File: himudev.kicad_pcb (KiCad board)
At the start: 4 copper layers, 93.6 x 43.6 mm, 132 parts, among them J1 USB_C16PIN, J2 M20-8770642R, J3 M20-8770642R, J4 20021121-00010C4LF, J5 M20-8762042, Q1 IRLML6402, Q2 BSS214NW, Q3 BSS214NW, Q4 BSS214NW, Q5 BSS214NW, Q6 BSS214NW, U1 FT230XS, U2 MCP1726-3302ESN, U3 MIC5319-1.8YD5-TR, U4 IS25WP032D, U5 FE310-G002, U6 ICM-20948, U7 BMP388, X1 KX2132709Z, Y1 TSX-3225 16.0000MF18X-AC0

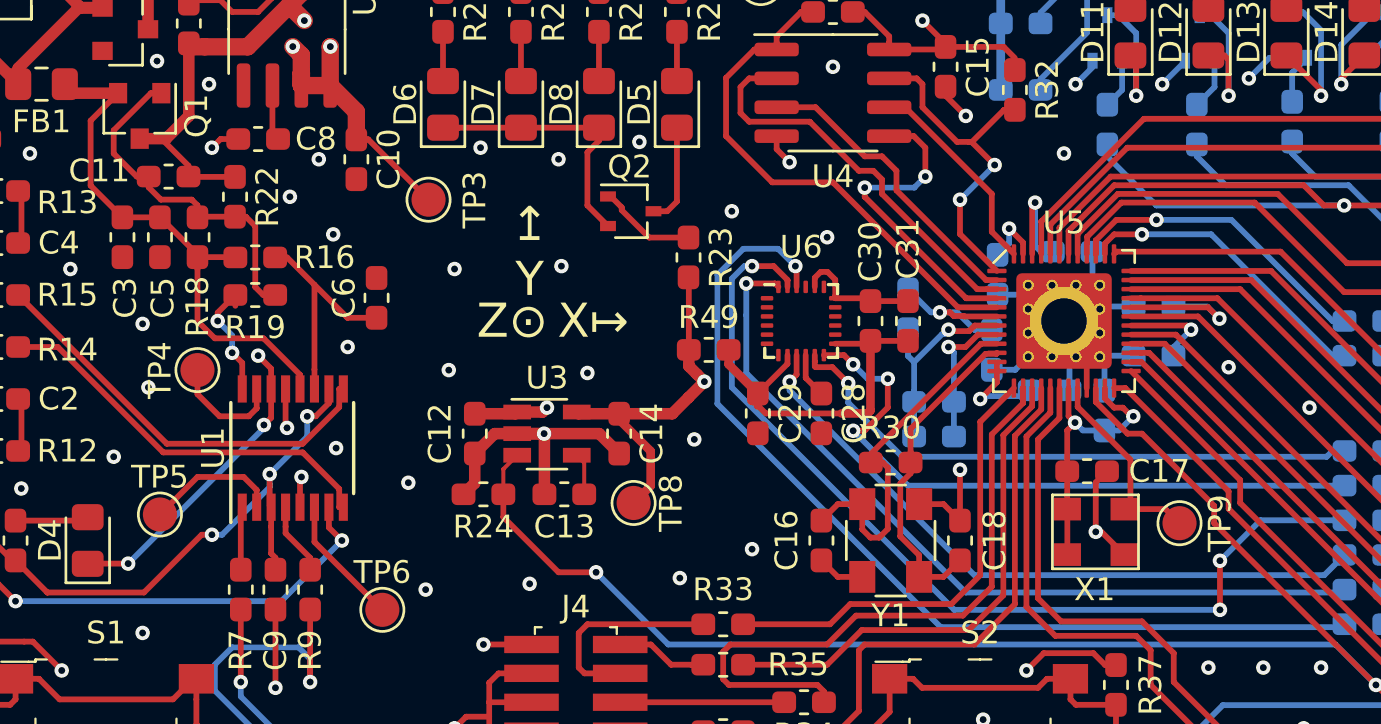
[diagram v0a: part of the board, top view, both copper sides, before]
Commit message: Made testpoint silkscreen more readable
Also, regenerated Gerber files.
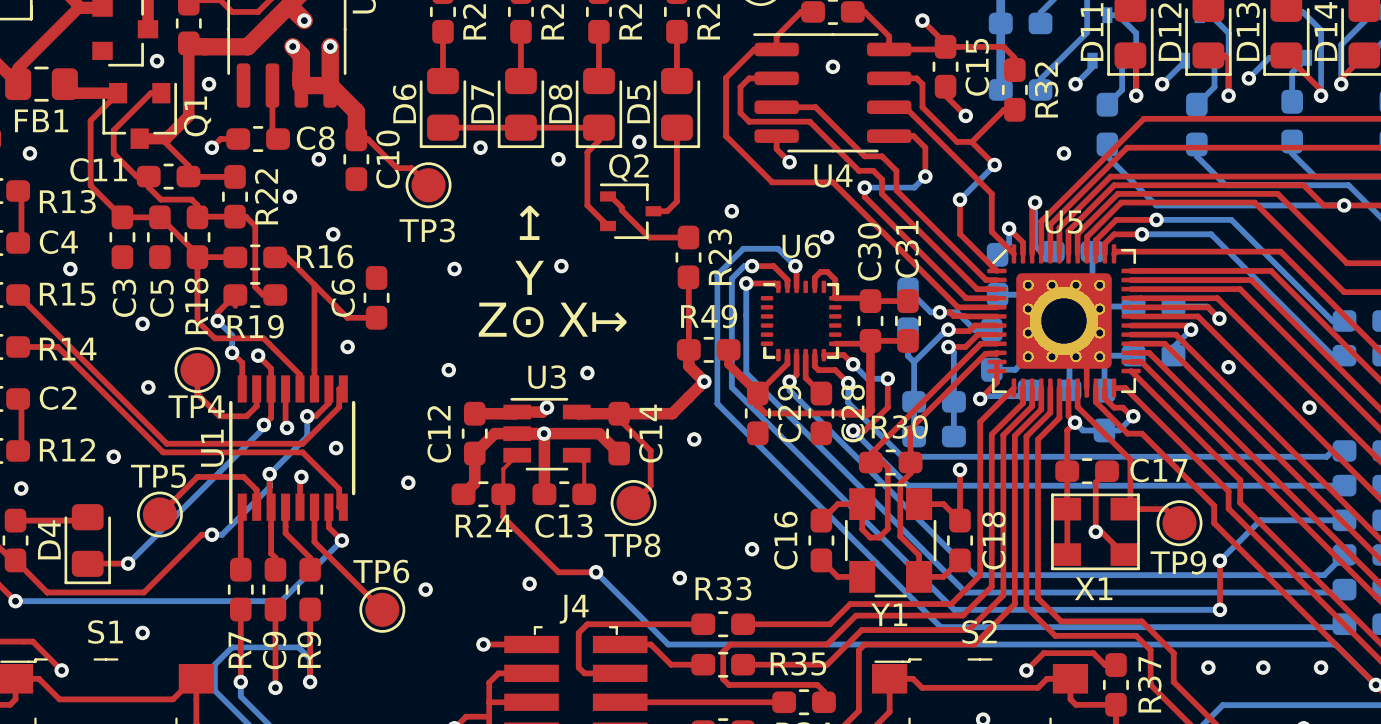
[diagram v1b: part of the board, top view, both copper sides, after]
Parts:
- moved TP3 0.64 mm to (136.0, 95.6), turned to 180 degrees
- turned TP4 to 180 degrees
- turned TP8 to 180 degrees
- turned TP9 to 180 degrees

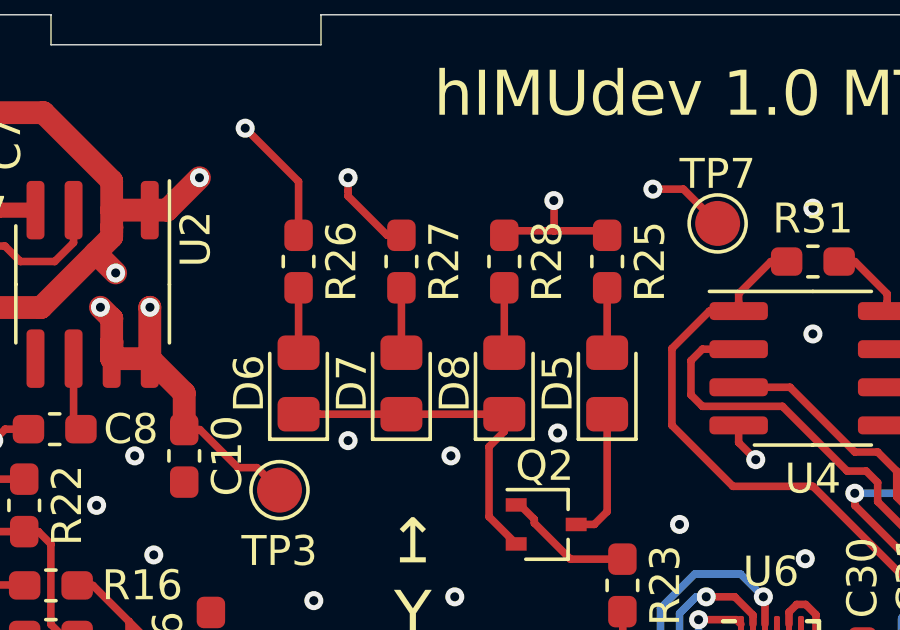
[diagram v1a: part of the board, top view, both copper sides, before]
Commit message: Reorder power LEDs in schematics, fix some USB-C DRC errors
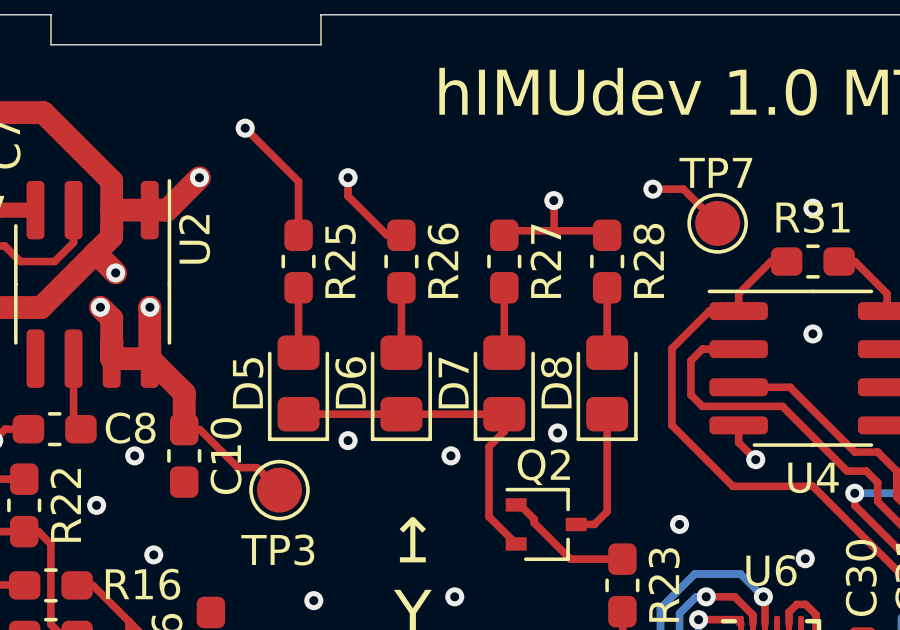
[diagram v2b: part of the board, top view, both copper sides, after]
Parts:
- J1: value USB_C16PIN -> USB-C-16PIN
- renumbered D6 to D5, D7 to D6, D8 to D7, D5 to D8, R26 to R25, R27 to R26, R28 to R27, R25 to R28

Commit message: Fix: exchange FTDI TX and RX diode colors
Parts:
- D3: value Green LTST-C170KGKT -> Orange LTST-C170KFKT
- D4: value Orange LTST-C170KFKT -> Green LTST-C170KGKT
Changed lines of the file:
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@@
       (effects (font (size 1 1) (thickness 0.15)))
     )
-    (fp_text value "Green LTST-C170KGKT" (at 0 1.65 90) (layer F.Fab)
+    (fp_text value "Orange LTST-C170KFKT" (at 0 1.65 90) (layer F.Fab)
       (effects (font (size 1 1) (thickness 0.15)))
     )
@@
       (effects (font (size 1 1) (thickness 0.15)))
     )
-    (fp_text value "Orange LTST-C170KFKT" (at 0 1.65 90) (layer F.Fab)
+    (fp_text value "Green LTST-C170KGKT" (at 0 1.65 90) (layer F.Fab)
       (effects (font (size 1 1) (thickness 0.15)))
     )

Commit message: Fix FTDI RX/TX diode designator
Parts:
- D3: value Orange LTST-C170KFKT -> Orange TX LTST-C170KFKT
- D4: value Green LTST-C170KGKT -> Green RX LTST-C170KGKT
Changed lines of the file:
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@@
       (effects (font (size 1 1) (thickness 0.15)))
     )
-    (fp_text value "Orange LTST-C170KFKT" (at 0 1.65 90) (layer F.Fab)
+    (fp_text value "Orange TX LTST-C170KFKT" (at 0 1.65 90) (layer F.Fab)
       (effects (font (size 1 1) (thickness 0.15)))
     )
@@
       (effects (font (size 1 1) (thickness 0.15)))
     )
-    (fp_text value "Green LTST-C170KGKT" (at 0 1.65 90) (layer F.Fab)
+    (fp_text value "Green RX LTST-C170KGKT" (at 0 1.65 90) (layer F.Fab)
       (effects (font (size 1 1) (thickness 0.15)))
     )

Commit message: Change resistor values to adjust LED brightness
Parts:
- R25: value 560 -> 1k
- R42: value 270 -> 560
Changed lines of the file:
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@@
       (effects (font (size 1 1) (thickness 0.15)))
     )
-    (fp_text value 560 (at 0 1.43 90) (layer F.Fab)
+    (fp_text value 1k (at 0 1.43 90) (layer F.Fab)
       (effects (font (size 1 1) (thickness 0.15)))
     )
@@
       (effects (font (size 1 1) (thickness 0.15)) (justify mirror))
     )
-    (fp_text value 270 (at 0 -1.43 180) (layer B.Fab)
-      (effects (font (size 1 1) (thickness 0.15)) (justify mirror))
-    )
+    (fp_text value 560 (at 0 -1.43 180) (layer B.Fab)
+      (effects (font (size 1 1) (thickness 0.15)) (justify mirror))
+    )

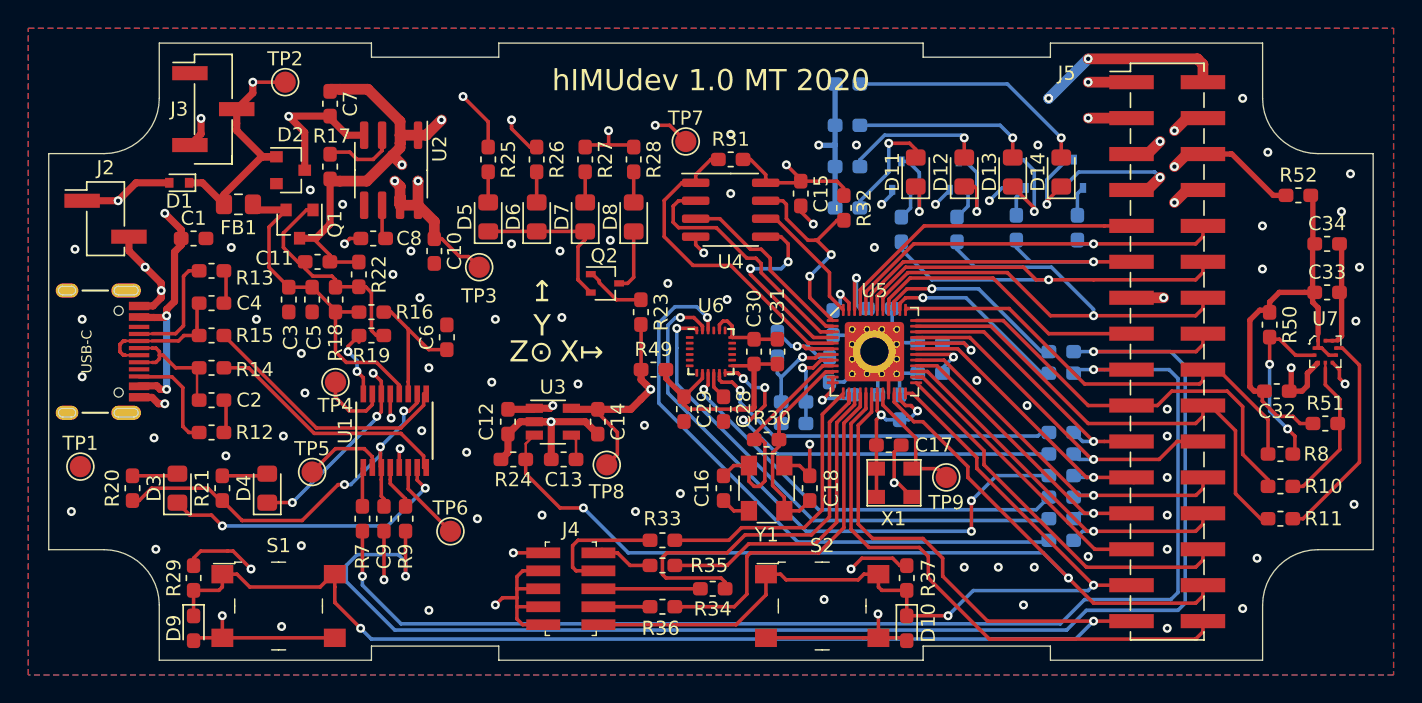
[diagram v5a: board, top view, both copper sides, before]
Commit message: Add 10k pull-downs on MCU LED outputs, improve layout
Pushed few traces, fixed DRC issue on one of the vias.
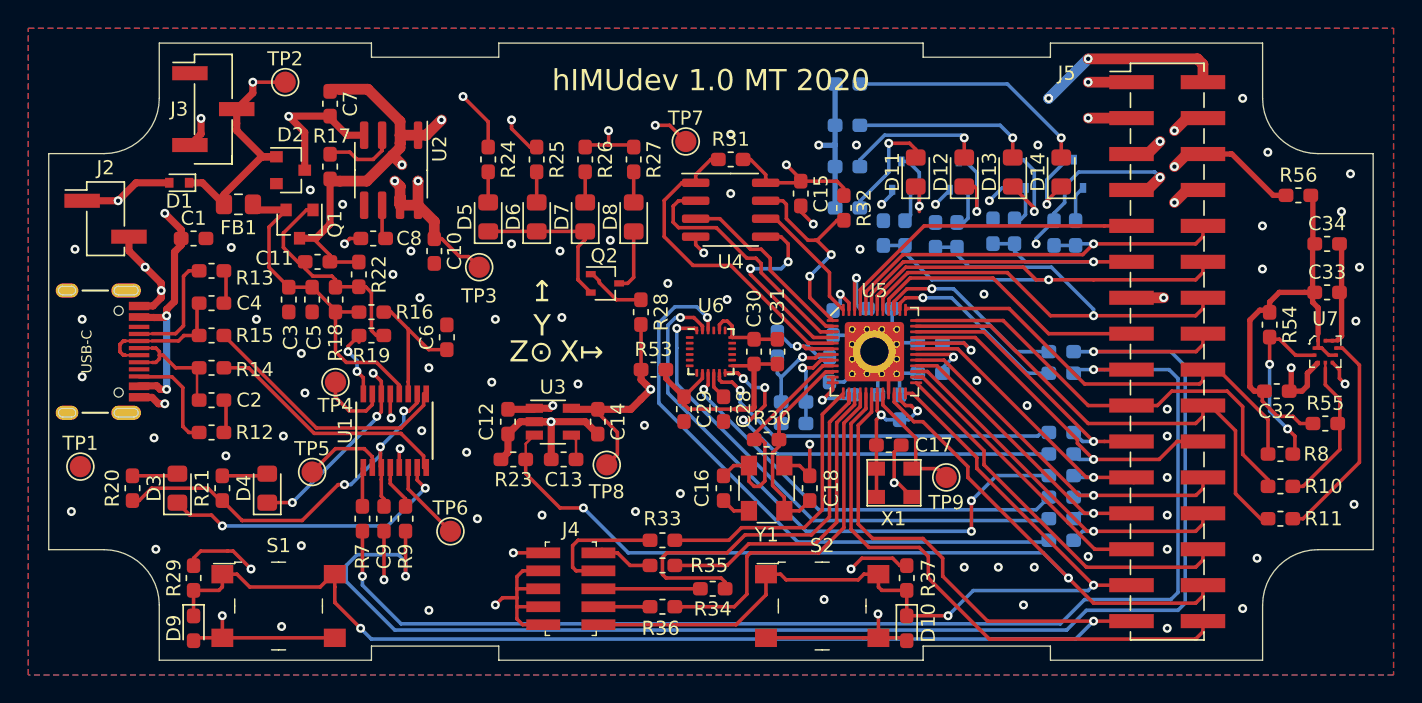
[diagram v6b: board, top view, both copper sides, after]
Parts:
- added R42: 10k, Resistor_SMD:R_0603_1608Metric_Pad1.05x0.95mm_HandSolder, B.Cu at (164.6, 93.2)
- added R45: 10k, Resistor_SMD:R_0603_1608Metric_Pad1.05x0.95mm_HandSolder, B.Cu at (168.3, 93.3)
- added R48: 10k, Resistor_SMD:R_0603_1608Metric_Pad1.05x0.95mm_HandSolder, B.Cu at (172.3, 93.1)
- added R51: 10k, Resistor_SMD:R_0603_1608Metric_Pad1.05x0.95mm_HandSolder, B.Cu at (176.7, 93.2)
- moved R50 0.40 mm to (178.2, 93.2)
- moved R44 0.38 mm to (169.8, 93.3)
- moved R41 0.36 mm to (166.1, 93.2)
- moved R47 0.28 mm to (173.9, 93.1)
- renumbered R24 to R23, R25 to R24, R26 to R25, R27 to R26, R28 to R27, R23 to R28, R42 to R43, R43 to R44, R44 to R46, R45 to R47, R46 to R49, R47 to R50, R48 to R52, R49 to R53, R50 to R54, R51 to R55, R52 to R56
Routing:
- net GND: track 197.5 -> 202.6 mm, vias 92 -> 94
- net /MCU_clk_reset/LED_4_YELLOW: track 28.7 -> 30.3 mm
- net /MCU_clk_reset/LED_3_BLUE: track 26.9 -> 28.4 mm
- net /MCU_clk_reset/LED_2_GREEN: track 38.8 -> 40.3 mm
- net /MCU_clk_reset/LED_1_RED: track 38.0 -> 39.2 mm
- net Net-(Q4-Pad1): track 2.26 -> 2.92 mm
- net Net-(Q5-Pad1): track 2.20 -> 2.79 mm

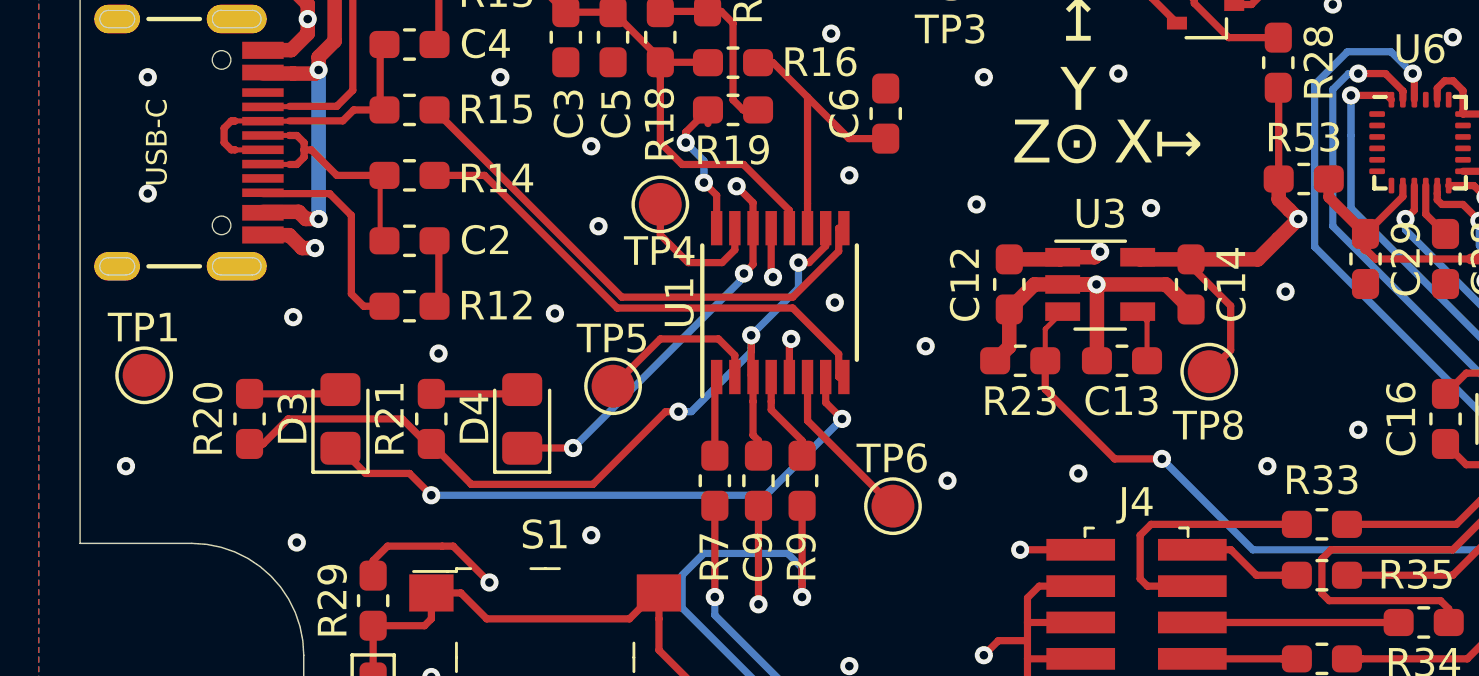
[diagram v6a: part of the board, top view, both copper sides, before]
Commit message: Switch places of D3 and D4
Also, fixed 1V8 via placement.
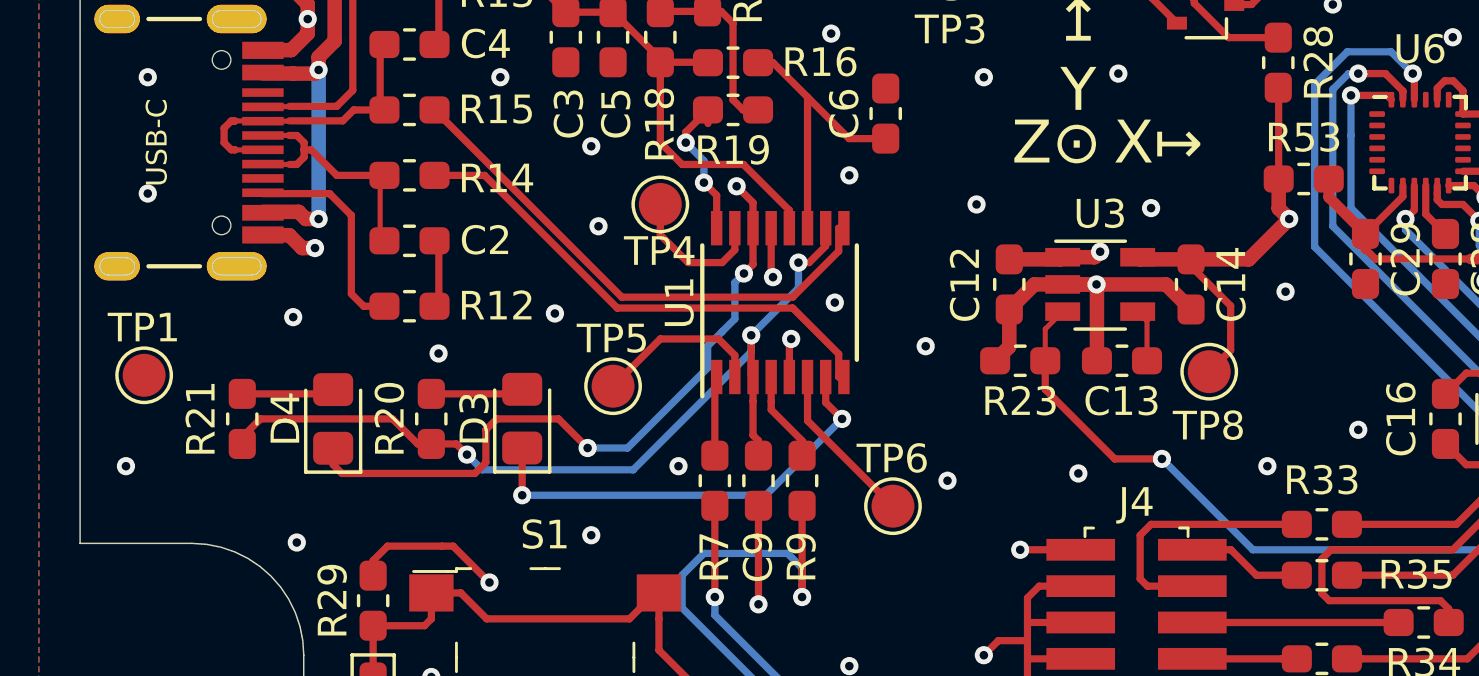
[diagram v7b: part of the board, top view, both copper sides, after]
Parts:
- moved D4 6.60 mm to (114.4, 111.3)
- moved R21 6.60 mm to (111.3, 111.3)
- moved D3 6.35 mm to (121.0, 111.2)
- moved R20 6.35 mm to (117.9, 111.3)
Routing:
- net Net-(D4-Pad1): track 13.8 -> 24.2 mm
- net Net-(D3-Pad1): track 21.0 -> 15.6 mm
- net GND: vias 94 -> 95
